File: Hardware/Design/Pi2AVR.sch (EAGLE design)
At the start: 15 parts, among them J1 Pi_40PIN, U7 ATMEGA328PB-AU, Y1 12MHz

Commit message: Hardware: add gnd to simple serial view
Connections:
- net 0V: now also J1.GND@3
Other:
- note added: "SET WEAK PULL-UP"
- moved on the sheet: R2
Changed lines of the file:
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@@
 <part name="J1" library="U-Pi" deviceset="RPI-ZERO" device="90" value="Pi_40PIN"/>
 <part name="C6" library="C-C" deviceset="C" device="C0603A" value=".1uF"/>
+<part name="GND1" library="Plane" deviceset="0V" device=""/>
 </parts>
 <sheets>
@@
 <text x="78.232" y="-14.224" size="1.778" layer="98">ISP</text>
 <text x="40.64" y="87.122" size="2.54" layer="98">AVR </text>
-<wire x1="114.808" y1="40.386" x2="106.934" y2="40.386" width="0.4064" layer="98"/>
-<wire x1="106.934" y1="40.386" x2="107.95" y2="41.148" width="0.4064" layer="98"/>
-<wire x1="106.934" y1="40.386" x2="107.95" y2="39.624" width="0.4064" layer="98"/>
 <text x="30.734" y="1.778" size="1.778" layer="98">* 328PB-AU PINOUT IS NOT
 SAME AS 328P-AU </text>
 <text x="13.462" y="-6.604" size="1.778" layer="98">12MHZ CRYSTAL:
 ECS-120-20-3X-TR</text>
-<wire x1="116.84" y1="43.18" x2="160.02" y2="43.18" width="0.1524" layer="98" style="shortdash"/>
-<wire x1="160.02" y1="17.78" x2="116.84" y2="17.78" width="0.1524" layer="98" style="shortdash"/>
+<wire x1="111.76" y1="43.18" x2="160.02" y2="43.18" width="0.1524" layer="98" style="shortdash"/>
+<wire x1="160.02" y1="17.78" x2="111.76" y2="17.78" width="0.1524" layer="98" style="shortdash"/>
 <wire x1="160.02" y1="43.18" x2="160.02" y2="17.78" width="0.1524" layer="98" style="shortdash"/>
 <text x="130.302" y="39.624" size="2.54" layer="98">PI SHUTDOWN</text>
-<wire x1="116.84" y1="43.18" x2="116.84" y2="17.78" width="0.1524" layer="98" style="shortdash"/>
+<wire x1="111.76" y1="43.18" x2="111.76" y2="17.78" width="0.1524" layer="98" style="shortdash"/>
 <text x="33.782" y="16.256" size="1.778" layer="98">*</text>
 <text x="82.804" y="54.61" size="1.778" layer="98">0</text>
@@
 <text x="83.058" y="23.622" size="1.778" layer="98">11</text>
 <text x="183.642" y="77.724" size="2.54" layer="98">PI ZERO [W], PI2, PI3</text>
+<text x="87.63" y="31.496" size="1.778" layer="98">SET WEAK PULL-UP</text>
 </plain>
 <instances>
@@
 <instance part="C5" gate="G$1" x="35.56" y="33.02"/>
 <instance part="S2" gate="S" x="137.16" y="25.4"/>
-<instance part="R2" gate="G$1" x="109.22" y="30.48" rot="R180"/>
+<instance part="R2" gate="G$1" x="119.38" y="30.48" rot="R180"/>
 <instance part="GND19" gate="1" x="149.86" y="22.86"/>
 <instance part="R3" gate="G$1" x="134.62" y="35.56" rot="R180"/>
 <instance part="J1" gate="G$1" x="200.66" y="38.1"/>
 <instance part="C6" gate="G$1" x="160.02" y="55.88" rot="R90"/>
+<instance part="GND1" gate="1" x="172.72" y="15.24"/>
 </instances>
 <busses>
@@
 <wire x1="142.24" y1="22.86" x2="142.24" y2="25.4" width="0.1524" layer="91"/>
 <junction x="142.24" y="25.4"/>
+</segment>
+<segment>
+<pinref part="GND1" gate="1" pin="0V"/>
+<wire x1="172.72" y1="17.78" x2="172.72" y2="20.32" width="0.1524" layer="91"/>
+<pinref part="J1" gate="G$1" pin="GND@3"/>
+<wire x1="172.72" y1="20.32" x2="177.8" y2="20.32" width="0.1524" layer="91"/>
 </segment>
 </net>
@@
 <segment>
 <pinref part="U7" gate="G$1" pin="(ICP1)PB0"/>
-<wire x1="104.14" y1="30.48" x2="78.74" y2="30.48" width="0.1524" layer="91"/>
+<wire x1="114.3" y1="30.48" x2="78.74" y2="30.48" width="0.1524" layer="91"/>
 <pinref part="R2" gate="G$1" pin="2"/>
 </segment>
@@
 <segment>
 <pinref part="R3" gate="G$1" pin="2"/>
-<wire x1="129.54" y1="35.56" x2="124.46" y2="35.56" width="0.1524" layer="91"/>
-<wire x1="124.46" y1="35.56" x2="124.46" y2="30.48" width="0.1524" layer="91"/>
+<wire x1="129.54" y1="35.56" x2="127" y2="35.56" width="0.1524" layer="91"/>
+<wire x1="127" y1="35.56" x2="127" y2="30.48" width="0.1524" layer="91"/>
 <pinref part="S2" gate="S" pin="2"/>
-<wire x1="124.46" y1="30.48" x2="124.46" y2="25.4" width="0.1524" layer="91"/>
-<wire x1="124.46" y1="25.4" x2="124.46" y2="22.86" width="0.1524" layer="91"/>
-<wire x1="124.46" y1="22.86" x2="132.08" y2="22.86" width="0.1524" layer="91"/>
+<wire x1="127" y1="30.48" x2="127" y2="25.4" width="0.1524" layer="91"/>
+<wire x1="127" y1="25.4" x2="127" y2="22.86" width="0.1524" layer="91"/>
+<wire x1="127" y1="22.86" x2="132.08" y2="22.86" width="0.1524" layer="91"/>
 <pinref part="S2" gate="S" pin="1"/>
-<wire x1="132.08" y1="25.4" x2="124.46" y2="25.4" width="0.1524" layer="91"/>
-<junction x="124.46" y="25.4"/>
+<wire x1="132.08" y1="25.4" x2="127" y2="25.4" width="0.1524" layer="91"/>
+<junction x="127" y="25.4"/>
 <pinref part="R2" gate="G$1" pin="1"/>
-<wire x1="114.3" y1="30.48" x2="124.46" y2="30.48" width="0.1524" layer="91"/>
-<junction x="124.46" y="30.48"/>
-</segment>
-</net>
+<wire x1="124.46" y1="30.48" x2="127" y2="30.48" width="0.1524" layer="91"/>
+<junction x="127" y="30.48"/>
+</segment>
+</net>

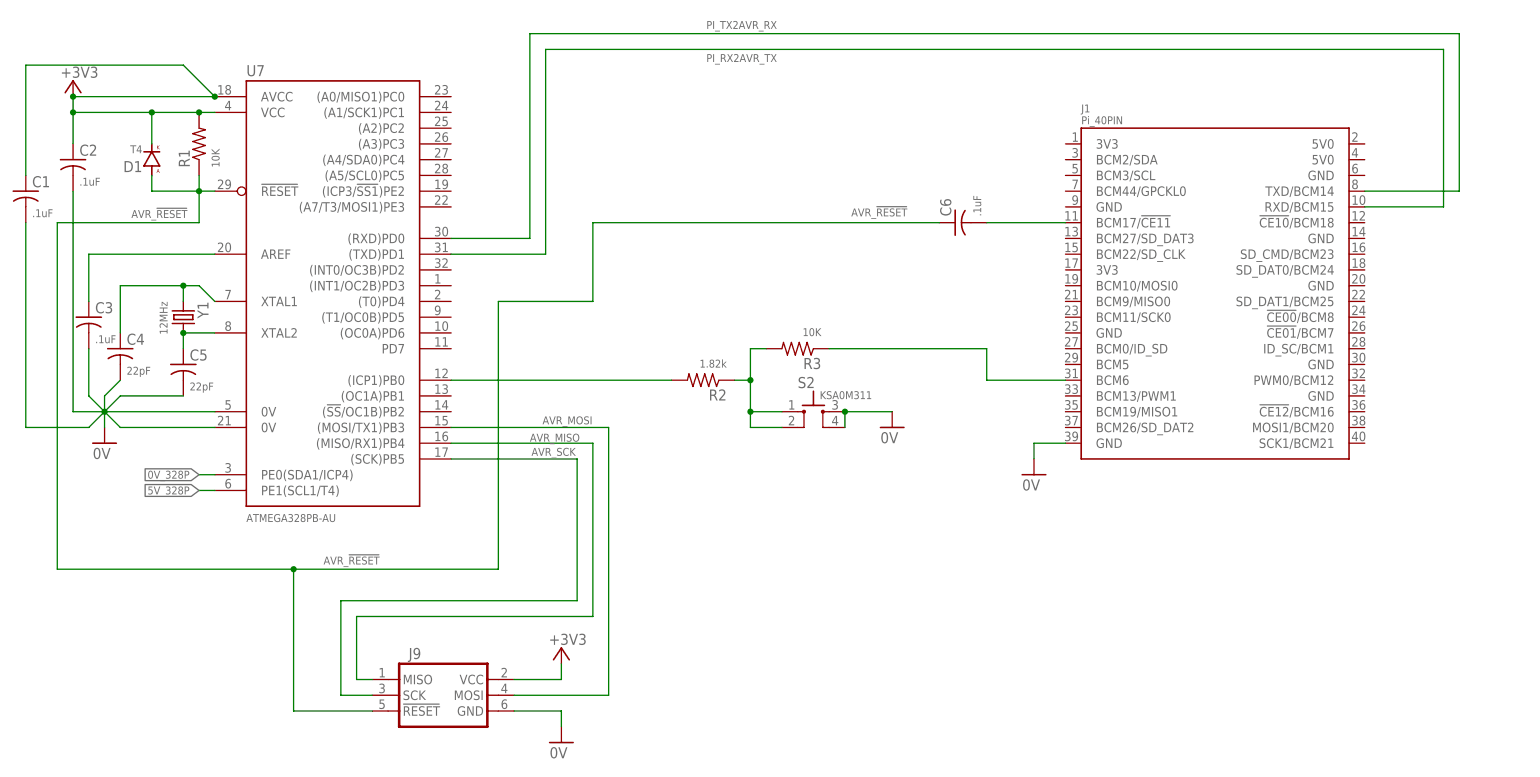
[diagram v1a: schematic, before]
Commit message: Hardware: remove weak pull-up from simple serial view
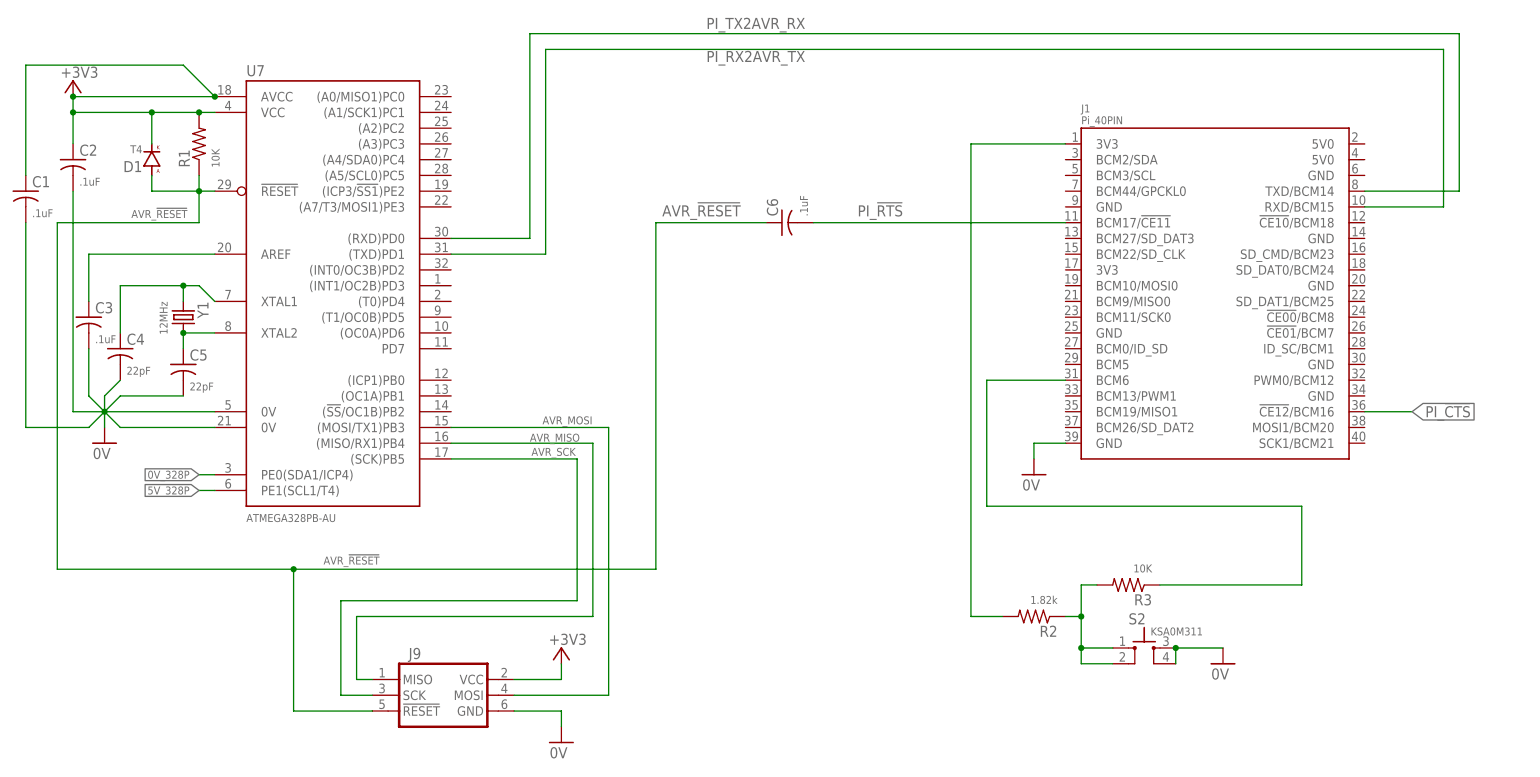
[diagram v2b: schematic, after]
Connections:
- net N$2 renamed PI_!RTS!
- removed net IO8: R2.2, U7.(ICP1)PB0
- new net 3V3@1: J1.3V3@1, R2.2
- new net PI_!CTS!: J1.!CE12!/BCM16
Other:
- note added: "AVR_!RESET!"
- note added: "BOOTLOADER: AVRDUDE CMD optiboot: -c arduino xboot: -c avr109"
- note added: "C6 = BOOTLOAD TRICK"
- note added: "C6 = BOOTLOAD TRICK WILL REST AVR WHEN SERIAL PORT OPEN"
- note added: "CLOSE"
- note added: "DIODE CLAMP WITH D1"
- note added: "OPEN"
- note added: "PI_!RTS!"
- note added: "PORT STATE"
- note removed: "8"
- note removed: "SET WEAK PULL-UP"
- moved on the sheet: C6, R2, R3, S2

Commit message: Hardware: add more info on pi2avr simple serial
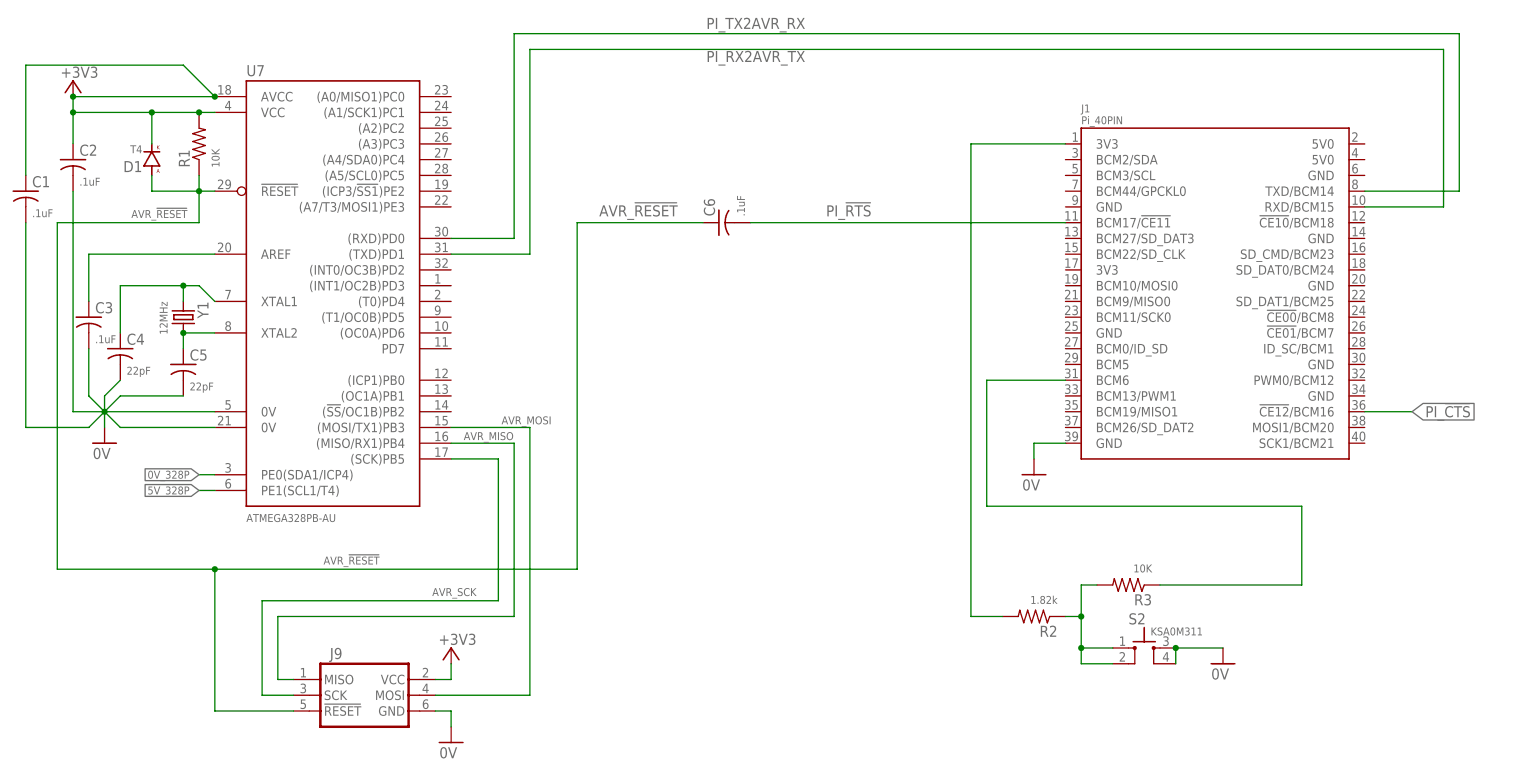
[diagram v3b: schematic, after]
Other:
- note added: "AVR RESET"
- note added: "BOOTLOADR RUNS"
- note added: "C Program to enable RTS and CTS https://github.com/epccs/RPUpi/tree/master/RPiRtsCts"
- note added: "C6 = BOOTLOAD TRICK RESET AVR WHEN PORT OPEN"
- note added: "CODE RUNS"
- note added: "D1 CLAMP"
- note added: "ISP TOOL NEEDED TO LOAD BOOTLOADER"
- note added: "PI SHUTDOWN WITH BCM6"
- note added: "Python Program to Halt Linux https://github.com/epccs/RPUpi/tree/master/Shutdown"
- note added: "optiboot: https://github.com/MCUdude/optiboot_flash xboot: https://github.com/alexforencich/xboot"
- note removed: "C6 = BOOTLOAD TRICK"
- note removed: "C6 = BOOTLOAD TRICK WILL REST AVR WHEN SERIAL PORT OPEN"
- note removed: "DIODE CLAMP WITH D1"
- note removed: "PI SHUTDOWN"
- moved on the sheet: C6, J9

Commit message: Hardware: ^4 schmatic design
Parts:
- U7: value ATMEGA328PB-AU -> ATMEGA328PB-A
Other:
- note added: "* 328PB-A PINOUT IS NOT SAME AS 328P-A"
- note removed: "* 328PB-AU PINOUT IS NOT SAME AS 328P-AU"
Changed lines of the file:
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@@
 <part name="D1" library="D-GP" deviceset="D" device="SOD123" value="T4"/>
 <part name="GND31" library="Plane" deviceset="0V" device=""/>
-<part name="U7" library="U-AVR" deviceset="ATMEGA328PB-AU" device="" value="ATMEGA328PB-AU"/>
+<part name="U7" library="U-AVR" deviceset="ATMEGA328PB-AU" device="" value="ATMEGA328PB-A"/>
 <part name="+3V1" library="Plane" deviceset="+3V3" device=""/>
 <part name="Y1" library="Y-XTL" deviceset="CSM" device="-3X" value="12MHz"/>
@@
 <text x="64.516" y="-12.954" size="1.778" layer="98">ISP</text>
 <text x="48.26" y="87.122" size="2.54" layer="98">AVR </text>
-<text x="30.734" y="1.778" size="1.778" layer="98">* 328PB-AU PINOUT IS NOT
-SAME AS 328P-AU </text>
+<text x="30.734" y="1.778" size="1.778" layer="98">* 328PB-A PINOUT IS NOT
+SAME AS 328P-A</text>
 <text x="13.462" y="-6.604" size="1.778" layer="98">12MHZ CRYSTAL:
 ECS-120-20-3X-TR</text>
